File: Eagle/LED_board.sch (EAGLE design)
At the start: 38 parts, among them P1 P1, P2 P2

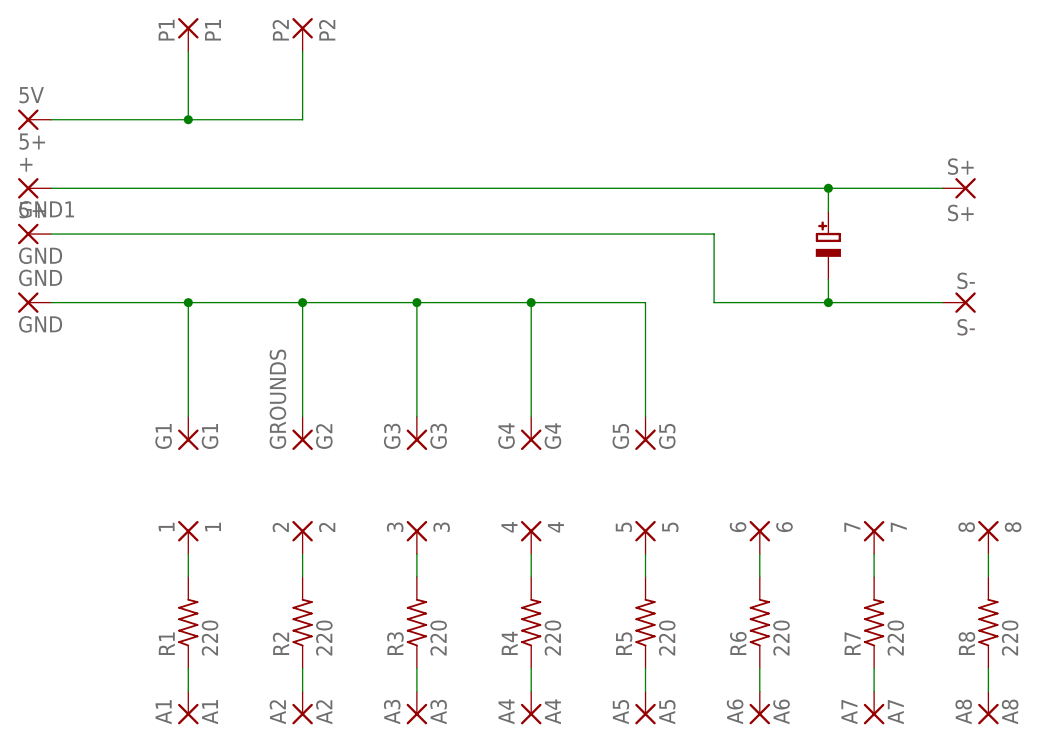
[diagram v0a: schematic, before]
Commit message: Changed the board design so it is cheaper at oshpark and no longer has the unused components
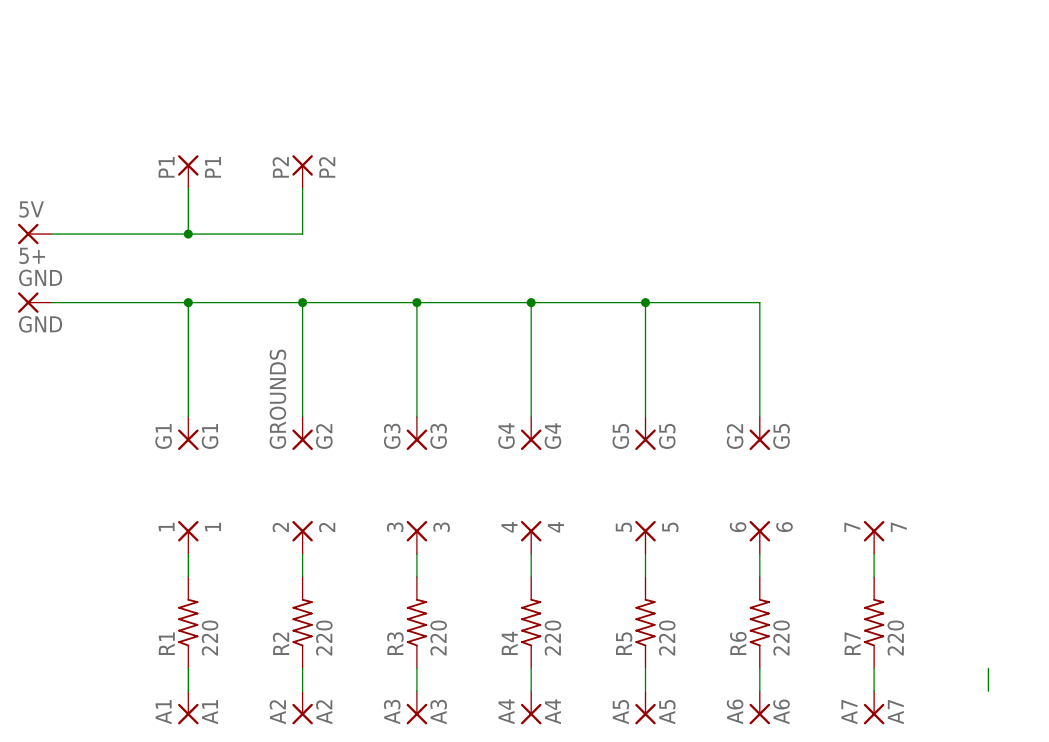
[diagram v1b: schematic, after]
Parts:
- removed +: 5+, wirepad:2,54/1,1
- removed 8: 8, wirepad:2,15/1,0
- removed A8: A8, wirepad:2,15/1,0
- removed C1: 480, CAP_ELECTROLYTIC:CAP_ELECTROLYTICPTH_3.5MMGRID_10MMDIA
- removed GND1: GND, wirepad:2,54/1,1
- removed R8: 220, resistor:R-US_0207/10
- removed S+: S+, wirepad:2,15/1,0
- removed S-: S-, wirepad:2,15/1,0
- added G2: G5, wirepad:2,15/1,0
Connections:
- removed net N$17: 8.P, R8.2
- removed net N$18: A8.P, R8.1
- removed net N$19: +.P, C1.+, S+.P
- removed net N$20: C1.-, GND1.P, S-.P
- net N$4: now also G2.P
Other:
- moved on the sheet: 5V, P1, P2
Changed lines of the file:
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@@
 <?xml version="1.0" encoding="utf-8"?>
 <!DOCTYPE eagle SYSTEM "eagle.dtd">
-<eagle version="7.7.0">
+<eagle version="8.5.2">
 <drawing>
 <settings>
-<setting alwaysvectorfont="yes"/>
+<setting alwaysvectorfont="no"/>
+<setting keepoldvectorfont="yes"/>
 <setting verticaltext="up"/>
 </settings>
@@
 <part name="GROUNDS" library="wirepad" deviceset="2,15/1,0" device="" value="G2"/>
 <part name="G1" library="wirepad" deviceset="2,15/1,0" device="" value="G1"/>
-<part name="R8" library="resistor" deviceset="R-US_" device="0207/10" value="220"/>
-<part name="8" library="wirepad" deviceset="2,15/1,0" device="" value="8"/>
-<part name="A8" library="wirepad" deviceset="2,15/1,0" device="" value="A8"/>
 <part name="G3" library="wirepad" deviceset="2,15/1,0" device="" value="G3"/>
 <part name="G4" library="wirepad" deviceset="2,15/1,0" device="" value="G4"/>
 <part name="G5" library="wirepad" deviceset="2,15/1,0" device="" value="G5"/>
 <part name="5V" library="wirepad" deviceset="2,54/1,1" device="" value="5+"/>
-<part name="C1" library="CAP_ELECTROLYTIC" deviceset="CAP_ELECTROLYTIC" device="PTH_3.5MMGRID_10MMDIA" value="480"/>
 <part name="P1" library="wirepad" deviceset="2,15/1,0" device="" value="P1"/>
 <part name="P2" library="wirepad" deviceset="2,15/1,0" device="" value="P2"/>
-<part name="S-" library="wirepad" deviceset="2,15/1,0" device="" value="S-"/>
-<part name="S+" library="wirepad" deviceset="2,15/1,0" device="" value="S+"/>
-<part name="+" library="wirepad" deviceset="2,54/1,1" device="" value="5+"/>
-<part name="GND1" library="wirepad" deviceset="2,54/1,1" device="" value="GND"/>
+<part name="G2" library="wirepad" deviceset="2,15/1,0" device="" value="G5"/>
 </parts>
 <sheets>
@@
 <instance part="GROUNDS" gate="1" x="10.16" y="60.96" rot="R90"/>
 <instance part="G1" gate="1" x="-2.54" y="60.96" rot="R90"/>
-<instance part="R8" gate="G$1" x="86.36" y="40.64" rot="R90"/>
-<instance part="8" gate="1" x="86.36" y="50.8" rot="R270"/>
-<instance part="A8" gate="1" x="86.36" y="30.48" rot="R90"/>
 <instance part="G3" gate="1" x="22.86" y="60.96" rot="R90"/>
 <instance part="G4" gate="1" x="35.56" y="60.96" rot="R90"/>
 <instance part="G5" gate="1" x="48.26" y="60.96" rot="R90"/>
-<instance part="5V" gate="1" x="-20.32" y="96.52"/>
-<instance part="C1" gate="G$1" x="68.58" y="81.28"/>
-<instance part="P1" gate="1" x="-2.54" y="106.68" rot="R270"/>
-<instance part="P2" gate="1" x="10.16" y="106.68" rot="R270"/>
-<instance part="S-" gate="1" x="83.82" y="76.2" rot="R180"/>
-<instance part="S+" gate="1" x="83.82" y="88.9" rot="R180"/>
-<instance part="+" gate="1" x="-20.32" y="88.9"/>
-<instance part="GND1" gate="1" x="-20.32" y="83.82"/>
+<instance part="5V" gate="1" x="-20.32" y="83.82"/>
+<instance part="P1" gate="1" x="-2.54" y="91.44" rot="R270"/>
+<instance part="P2" gate="1" x="10.16" y="91.44" rot="R270"/>
+<instance part="G2" gate="1" x="60.96" y="60.96" rot="R90"/>
 </instances>
 <busses>
@@
 </segment>
 </net>
-<net name="N$17" class="0">
-<segment>
-<pinref part="8" gate="1" pin="P"/>
-<pinref part="R8" gate="G$1" pin="2"/>
-<wire x1="86.36" y1="48.26" x2="86.36" y2="45.72" width="0.1524" layer="91"/>
-</segment>
-</net>
 <net name="N$18" class="0">
 <segment>
-<pinref part="R8" gate="G$1" pin="1"/>
-<pinref part="A8" gate="1" pin="P"/>
 <wire x1="86.36" y1="35.56" x2="86.36" y2="33.02" width="0.1524" layer="91"/>
 </segment>
@@
 <junction x="22.86" y="76.2"/>
 <junction x="35.56" y="76.2"/>
+<wire x1="48.26" y1="76.2" x2="60.96" y2="76.2" width="0.1524" layer="91"/>
+<pinref part="G2" gate="1" pin="P"/>
+<wire x1="60.96" y1="76.2" x2="60.96" y2="63.5" width="0.1524" layer="91"/>
+<junction x="48.26" y="76.2"/>
 </segment>
 </net>
@@
 <segment>
 <pinref part="P2" gate="1" pin="P"/>
-<wire x1="10.16" y1="104.14" x2="10.16" y2="96.52" width="0.1524" layer="91"/>
-<wire x1="-2.54" y1="96.52" x2="10.16" y2="96.52" width="0.1524" layer="91"/>
+<wire x1="10.16" y1="88.9" x2="10.16" y2="83.82" width="0.1524" layer="91"/>
+<wire x1="-2.54" y1="83.82" x2="10.16" y2="83.82" width="0.1524" layer="91"/>
 <pinref part="P1" gate="1" pin="P"/>
-<wire x1="-2.54" y1="104.14" x2="-2.54" y2="96.52" width="0.1524" layer="91"/>
-<junction x="-2.54" y="96.52"/>
+<wire x1="-2.54" y1="88.9" x2="-2.54" y2="83.82" width="0.1524" layer="91"/>
+<junction x="-2.54" y="83.82"/>
 <pinref part="5V" gate="1" pin="P"/>
-<wire x1="-17.78" y1="96.52" x2="-2.54" y2="96.52" width="0.1524" layer="91"/>
-</segment>
-</net>
-<net name="N$19" class="0">
-<segment>
-<pinref part="S+" gate="1" pin="P"/>
-<wire x1="68.58" y1="88.9" x2="81.28" y2="88.9" width="0.1524" layer="91"/>
-<pinref part="C1" gate="G$1" pin="+"/>
-<wire x1="68.58" y1="86.36" x2="68.58" y2="88.9" width="0.1524" layer="91"/>
-<pinref part="+" gate="1" pin="P"/>
-<wire x1="-17.78" y1="88.9" x2="68.58" y2="88.9" width="0.1524" layer="91"/>
-<junction x="68.58" y="88.9"/>
-</segment>
-</net>
-<net name="N$20" class="0">
-<segment>
-<pinref part="S-" gate="1" pin="P"/>
-<wire x1="68.58" y1="76.2" x2="81.28" y2="76.2" width="0.1524" layer="91"/>
-<pinref part="C1" gate="G$1" pin="-"/>
-<wire x1="68.58" y1="78.74" x2="68.58" y2="76.2" width="0.1524" layer="91"/>
-<pinref part="GND1" gate="1" pin="P"/>
-<wire x1="-17.78" y1="83.82" x2="55.88" y2="83.82" width="0.1524" layer="91"/>
-<wire x1="55.88" y1="83.82" x2="55.88" y2="76.2" width="0.1524" layer="91"/>
-<wire x1="55.88" y1="76.2" x2="68.58" y2="76.2" width="0.1524" layer="91"/>
-<junction x="68.58" y="76.2"/>
+<wire x1="-17.78" y1="83.82" x2="-2.54" y2="83.82" width="0.1524" layer="91"/>
 </segment>
 </net>
@@
 </schematic>
 </drawing>
-<compatibility>
-<note version="6.3" minversion="6.2.2" severity="warning">
-Since Version 6.2.2 text objects can contain more than one line,
-which will not be processed correctly with this version.
-</note>
-</compatibility>
 </eagle>
